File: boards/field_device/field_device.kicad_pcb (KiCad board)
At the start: 4 copper layers, 58 parts, among them J1 Conn_01x05_Pin, SW1 SW_SPST, U1 CHT20MEMS, U2 STM32C051F6P6, U3 SPA06-003, U4 CN3163, U5 HX8001-AJC, U6 SX1262IMLTRT, Y1 Crystal_GND24

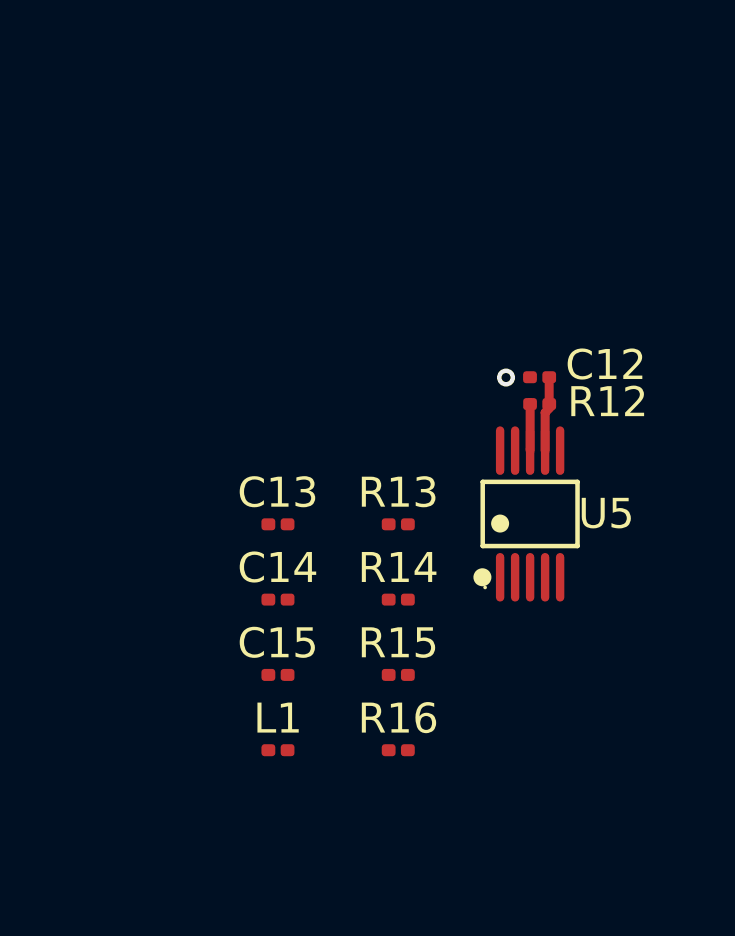
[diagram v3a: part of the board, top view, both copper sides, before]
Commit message: added sources + some pcb routing
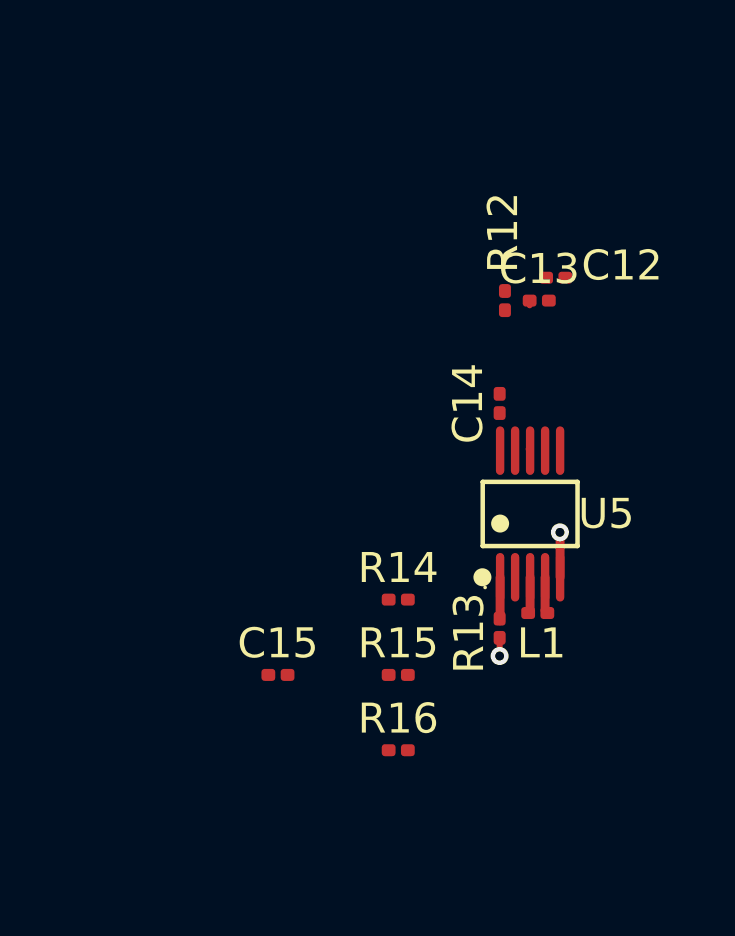
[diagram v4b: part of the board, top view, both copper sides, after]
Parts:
- moved C13 11.5 mm to (204.8, 79.2)
- moved C14 9.87 mm to (203.5, 82.7), turned to 90 degrees
- moved L1 9.79 mm to (204.7, 89.7), turned to 180 degrees
- moved R13 4.84 mm to (203.5, 90.2), turned to -90 degrees
- moved R12 3.64 mm to (203.6, 79.2), turned to -90 degrees
- moved C12 3.36 mm to (205.3, 78.5)
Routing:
- net /power_source/regulator/pwr: track 2.39 -> 0.05 mm
- net GND: track 0.00 -> 2.23 mm, vias 0 -> 2
- net /power_source/regulator/enable: track 1.71 -> 0.23 mm
- net Net-(U5-RT): track 0.00 -> 1.48 mm
- net Net-(U5-SW2): track 0.00 -> 1.22 mm
- net Net-(U5-SW1): track 0.00 -> 1.22 mm
- net (no net): vias 1 -> 0
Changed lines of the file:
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@@
 	(footprint "Capacitor_SMD:C_0201_0603Metric"
 		(layer "F.Cu")
-		(at 196.065 86.705)
+		(at 204.7748 79.248)
 		(descr "Capacitor SMD 0201 (0603 Metric), square (rectangular) end terminal, IPC-7351 nominal, (Body size source: https://www.vishay.com/docs/20052/crcw0201e3.pdf)")
 		(tags "capacitor")
@@
 		(property "Value" "100nF"
 			(at 0 1.05 0)
-			(layer "F.Fab")
+			(layer "B.Fab")
 			(effects
 				(font
@@
 					(thickness 0.15)
 				)
+				(justify mirror)
 			)
 		)
@@
 	(footprint "Resistor_SMD:R_0201_0603Metric"
 		(layer "F.Cu")
-		(at 204.787849 82.697014 180)
+		(at 203.6318 79.248 -90)
 		(descr "Resistor SMD 0201 (0603 Metric), square (rectangular) end terminal, IPC-7351 nominal, (Body size source: https://www.vishay.com/docs/20052/crcw0201e3.pdf)")
 		(tags "resistor")
 		(property "Reference" "R12"
-			(at -2.26994 0.060373 0)
+			(at -2.26994 0.060373 90)
 			(layer "F.SilkS")
 			(effects
@@
 		)
 		(property "Value" "1MΩ"
-			(at 0 1.05 0)
+			(at 0 1.05 90)
 			(layer "F.Fab")
 			(effects
@@
 		)
 		(property "Datasheet" ""
-			(at 0 0 0)
+			(at 0 0 90)
 			(layer "F.Fab")
 			(hide yes)
@@
 		)
 		(property "Description" "Resistor"
-			(at 0 0 0)
+			(at 0 0 90)
 			(layer "F.Fab")
 			(hide yes)
@@
 		)
 		(property "KiLib_Generator" "SMD_2terminal_chip_molded"
-			(at 0 0 0)
+			(at 0 0 90)
 			(layer "F.SilkS")
 			(hide yes)
@@
 		)
 		(fp_text user "${REFERENCE}"
-			(at 0 -0.68 0)
+			(at 0 -0.68 90)
 			(layer "F.Fab")
 			(effects
@@
 		)
 		(pad "" smd roundrect
-			(at -0.345 0 180)
+			(at -0.345 0 270)
 			(size 0.318 0.36)
 			(layers "F.Paste")
@@
 		)
 		(pad "" smd roundrect
-			(at 0.345 0 180)
+			(at 0.345 0 270)
 			(size 0.318 0.36)
 			(layers "F.Paste")
@@
 		)
 		(pad "1" smd roundrect
-			(at -0.32 0 180)
+			(at -0.32 0 270)
 			(size 0.46 0.4)
 			(layers "F.Cu" "F.Mask")
@@
 		)
 		(pad "2" smd roundrect
-			(at 0.32 0 180)
+			(at 0.32 0 270)
 			(size 0.46 0.4)
 			(layers "F.Cu" "F.Mask")
@@
 	(footprint "Capacitor_SMD:C_0201_0603Metric"
 		(layer "F.Cu")
-		(at 196.065 89.215)
+		(at 203.454 82.677 90)
 		(descr "Capacitor SMD 0201 (0603 Metric), square (rectangular) end terminal, IPC-7351 nominal, (Body size source: https://www.vishay.com/docs/20052/crcw0201e3.pdf)")
 		(tags "capacitor")
 		(property "Reference" "C14"
-			(at 0 -1.05 0)
+			(at 0 -1.05 90)
 			(layer "F.SilkS")
 			(effects
@@
 		)
 		(property "Value" "1.5nF"
-			(at 0 1.05 0)
+			(at 0 1.05 90)
 			(layer "F.Fab")
 			(effects
@@
 		)
 		(property "Datasheet" ""
-			(at 0 0 0)
+			(at 0 0 90)
 			(layer "F.Fab")
 			(hide yes)
@@
 		)
 		(property "Description" "Unpolarized capacitor"
-			(at 0 0 0)
+			(at 0 0 90)
 			(layer "F.Fab")
 			(hide yes)
@@
 		)
 		(property "KiLib_Generator" "SMD_2terminal_chip_molded"
-			(at 0 0 0)
+			(at 0 0 90)
 			(layer "F.SilkS")
 			(hide yes)
@@
 		)
 		(fp_text user "${REFERENCE}"
-			(at 0 -0.68 0)
+			(at 0 -0.68 90)
 			(layer "F.Fab")
 			(effects
@@
 		)
 		(pad "" smd roundrect
-			(at -0.345 0)
+			(at -0.345 0 90)
 			(size 0.318 0.36)
 			(layers "F.Paste")
@@
 		)
 		(pad "" smd roundrect
-			(at 0.345 0)
+			(at 0.345 0 90)
 			(size 0.318 0.36)
 			(layers "F.Paste")
@@
 		)
 		(pad "1" smd roundrect
-			(at -0.32 0)
+			(at -0.32 0 90)
 			(size 0.46 0.4)
 			(layers "F.Cu" "F.Mask")
@@
 		)
 		(pad "2" smd roundrect
-			(at 0.32 0)
+			(at 0.32 0 90)
 			(size 0.46 0.4)
 			(layers "F.Cu" "F.Mask")
@@
 	(footprint "Capacitor_SMD:C_0201_0603Metric"
 		(layer "F.Cu")
-		(at 204.785554 81.803054 180)
+		(at 205.323 78.486 180)
 		(descr "Capacitor SMD 0201 (0603 Metric), square (rectangular) end terminal, IPC-7351 nominal, (Body size source: https://www.vishay.com/docs/20052/crcw0201e3.pdf)")
 		(tags "capacitor")
@@
 	(footprint "Inductor_SMD:L_0201_0603Metric"
 		(layer "F.Cu")
-		(at 196.065 94.235)
+		(at 204.724 89.662 180)
 		(descr "Inductor SMD 0201 (0603 Metric), square (rectangular) end terminal, IPC-7351 nominal, (Body size source: https://www.vishay.com/docs/20052/crcw0201e3.pdf)")
 		(tags "inductor")
 		(property "Reference" "L1"
-			(at 0 -1.05 0)
+			(at -0.127 -1.016 0)
 			(layer "F.SilkS")
 			(effects
@@
 		)
 		(pad "" smd roundrect
-			(at -0.345 0)
+			(at -0.345 0 180)
 			(size 0.318 0.36)
 			(layers "F.Paste")
@@
 		)
 		(pad "" smd roundrect
-			(at 0.345 0)
+			(at 0.345 0 180)
 			(size 0.318 0.36)
 			(layers "F.Paste")
@@
 		)
 		(pad "1" smd roundrect
-			(at -0.32 0)
+			(at -0.32 0 180)
 			(size 0.46 0.4)
 			(layers "F.Cu" "F.Mask")
@@
 		)
 		(pad "2" smd roundrect
-			(at 0.32 0)
+			(at 0.32 0 180)
 			(size 0.46 0.4)
 			(layers "F.Cu" "F.Mask")
@@
 	(footprint "Resistor_SMD:R_0201_0603Metric"
 		(layer "F.Cu")
-		(at 200.075 86.705)
+		(at 203.454 90.17 -90)
 		(descr "Resistor SMD 0201 (0603 Metric), square (rectangular) end terminal, IPC-7351 nominal, (Body size source: https://www.vishay.com/docs/20052/crcw0201e3.pdf)")
 		(tags "resistor")
 		(property "Reference" "R13"
-			(at 0 -1.05 0)
+			(at 0.163 1.016 90)
 			(layer "F.SilkS")
 			(effects
@@
 		)
 		(property "Value" "60.4kΩ"
-			(at 0 1.05 0)
+			(at 0 1.05 90)
 			(layer "F.Fab")
 			(effects
@@
 		)
 		(property "Datasheet" ""
-			(at 0 0 0)
+			(at 0 0 90)
 			(layer "F.Fab")
 			(hide yes)
@@
 		)
 		(property "Description" "Resistor"
-			(at 0 0 0)
+			(at 0 0 90)
 			(layer "F.Fab")
 			(hide yes)
@@
 		)
 		(property "KiLib_Generator" "SMD_2terminal_chip_molded"
-			(at 0 0 0)
+			(at 0 0 90)
 			(layer "F.SilkS")
 			(hide yes)
@@
 		)
 		(fp_text user "${REFERENCE}"
-			(at 0 -0.68 0)
+			(at 0 -0.68 90)
 			(layer "F.Fab")
 			(effects
@@
 		)
 		(pad "" smd roundrect
-			(at -0.345 0)
+			(at -0.345 0 270)
 			(size 0.318 0.36)
 			(layers "F.Paste")
@@
 		)
 		(pad "" smd roundrect
-			(at 0.345 0)
+			(at 0.345 0 270)
 			(size 0.318 0.36)
 			(layers "F.Paste")
@@
 		)
 		(pad "1" smd roundrect
-			(at -0.32 0)
+			(at -0.32 0 270)
 			(size 0.46 0.4)
 			(layers "F.Cu" "F.Mask")
@@
 		)
 		(pad "2" smd roundrect
-			(at 0.32 0)
+			(at 0.32 0 270)
 			(size 0.46 0.4)
 			(layers "F.Cu" "F.Mask")
@@
 		)
 	)
-	(via blind
-		(at 203.667585 81.812532)
-		(size 0.6)
-		(drill 0.3)
-		(layers "F.Cu" "In1.Cu")
-		(net "")
+	(segment
+		(start 204.9572 84.2372)
+		(end 204.97 84.25)
+		(width 0.2)
+		(layer "F.Cu")
+		(net "/power_source/regulator/pwr")
 	)
 	(segment
-		(start 205.105554 81.803054)
-		(end 205.105554 82.694719)
-		(width 0.3)
+		(start 204.9932 84.2268)
+		(end 204.97 84.25)
+		(width 0.2)
 		(layer "F.Cu")
 		(net "/power_source/regulator/pwr")
 	)
 	(segment
-		(start 205.132849 82.818361)
-		(end 204.97 82.98121)
+		(start 205.47 87.138)
+		(end 205.47 88.47)
 		(width 0.3)
 		(layer "F.Cu")
-		(net "/power_source/regulator/pwr")
+		(net "GND")
+	)
+	(segment
+		(start 205.463539 86.973212)
+		(end 205.463539 87.131539)
+		(width 0.3)
+		(layer "F.Cu")
+		(net "GND")
 	)
 	(segment
-		(start 205.105554 82.694719)
-		(end 205.107849 82.697014)
+		(start 203.454 90.581)
+		(end 203.454 91.186)
 		(width 0.2)
 		(layer "F.Cu")
-		(net "/power_source/regulator/pwr")
+		(net "GND")
 	)
 	(segment
-		(start 204.97 82.98121)
-		(end 204.97 84.25)
+		(start 205.463539 87.131539)
+		(end 205.47 87.138)
 		(width 0.3)
 		(layer "F.Cu")
-		(net "/power_source/regulator/pwr")
+		(net "GND")
+	)
+	(segment
+		(start 205.0948 78.5778)
+		(end 205.003 78.486)
+		(width 0.2)
+		(layer "F.Cu")
+		(net "GND")
+	)
+	(via blind
+		(at 203.454 91.095)
+		(size 0.6)
+		(drill 0.3)
+		(layers "F.Cu" "In1.Cu")
+		(net "GND")
+	)
+	(via blind
+		(at 205.463539 86.973212)
+		(size 0.6)
+		(drill 0.3)
+		(layers "F.Cu" "In1.Cu")
+		(net "GND")
 	)
 	(segment
@@
 	)
 	(segment
-		(start 204.47 82.641211)
-		(end 204.492849 82.618362)
+		(start 204.4548 79.248)
+		(end 204.4548 79.406456)
 		(width 0.2)
 		(layer "F.Cu")
@@
 	)
 	(segment
-		(start 204.47 84.25)
-		(end 204.47 82.641211)
+		(start 204.97 88.47)
+		(end 204.97 89.588)
 		(width 0.3)
 		(layer "F.Cu")
-		(net "/power_source/regulator/enable")
+		(net "Net-(U5-SW2)")
+	)
+	(segment
+		(start 204.97 89.588)
+		(end 205.044 89.662)
+		(width 0.2)
+		(layer "F.Cu")
+		(net "Net-(U5-SW2)")
+	)
+	(segment
+		(start 204.47 89.596)
+		(end 204.404 89.662)
+		(width 0.2)
+		(layer "F.Cu")
+		(net "Net-(U5-SW1)")
+	)
+	(segment
+		(start 204.47 88.47)
+		(end 204.47 89.596)
+		(width 0.3)
+		(layer "F.Cu")
+		(net "Net-(U5-SW1)")
+	)
+	(segment
+		(start 203.47 88.47)
+		(end 203.47 89.925)
+		(width 0.3)
+		(layer "F.Cu")
+		(net "Net-(U5-RT)")
+	)
+	(segment
+		(start 203.47 89.925)
+		(end 203.454 89.941)
+		(width 0.2)
+		(layer "F.Cu")
+		(net "Net-(U5-RT)")
 	)
 	(zone

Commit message: i guess made schematic more readable?
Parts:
- removed C24: C_Shunt_1, Capacitor_SMD:C_0603_1608Metric
- removed C25: C_Shunt_2, Capacitor_SMD:C_0603_1608Metric
- removed D1: LED, LED_SMD:LED_0603_1608Metric
- removed L1: 10uH, Inductor_SMD:L_0201_0603Metric
- removed R10: 1kΩ, Resistor_SMD:R_0603_1608Metric
- removed R15: 15kΩ, Resistor_SMD:R_0201_0603Metric
- removed R16: 200kΩ, Resistor_SMD:R_0201_0603Metric
- removed R5: 10kΩ, Resistor_SMD:R_0603_1608Metric
- removed R9: 10kΩ?, Resistor_SMD:R_0603_1608Metric
- added D3: GREEN, LED_SMD:LED_0603_1608Metric, F.Cu at (32.8, 48.1)
- added J2: Conn_01x02_Pin, Connector_PinHeader_1.00mm:PinHeader_1x02_P1.00mm_Vertical, F.Cu at (39.7, 13.3)
- C1: value 10uF -> 10u
- C10: value 1uF -> 10u; footprint Capacitor_SMD:C_0603_1608Metric -> Capacitor_SMD:C_0201_0603Metric
- C11: value 1uF -> 100n; footprint Capacitor_SMD:C_0603_1608Metric -> Sensor_Current:LEM_HX02-P
- C12: value 10uF -> 22u; footprint Capacitor_SMD:C_0201_0603Metric -> Sensor_Current:LEM_HX02-P
- C13: value 100nF -> 1n5; footprint Capacitor_SMD:C_0201_0603Metric -> Sensor_Current:LEM_HX02-P
- C14: value 1.5nF -> 10uF; footprint Capacitor_SMD:C_0201_0603Metric -> Capacitor_SMD:C_0603_1608Metric
- C15: value 22uF -> 100nF; footprint Capacitor_SMD:C_0201_0603Metric -> Capacitor_SMD:C_0603_1608Metric
- C16: value 470nF -> 100nF
- C17: value 10uF -> 100nF
- C18: value 100nF -> 470nF
- C19: value 100nF -> 47nF
- C2: value 4.7uF -> 100n
- C20: value 100nF -> 100pF
- C21: value 47nF -> 100pF
- C22: value 100pF -> C_Shunt_1
- C23: value 100pF -> C_Shunt_2
- C3: value 100nF -> 10u
- C4, C5, C6, C7: value 100nF -> 100n
- C8, C9: value 100nF -> 1u
- D2: value LED -> ORANGE
- R1: value 330Ω -> 330R
- R11: value 2kΩ -> 10k
- R12: value 1MΩ -> 10k?; footprint Resistor_SMD:R_0201_0603Metric -> Resistor_SMD:R_0603_1608Metric
- R13: value 60.4kΩ -> 1kΩ; footprint Resistor_SMD:R_0201_0603Metric -> Resistor_SMD:R_0603_1608Metric
- R14: value 340kΩ -> 1k5; footprint Resistor_SMD:R_0201_0603Metric -> Resistor_SMD:R_0603_1608Metric
- R2: value 10kΩ? -> 10k
- R3: value 10kΩ -> 10k
- R4: value 10kΩ -> 10k?
- R6, R7, R8: value 22Ω -> 22R
- U2: value STM32C051F6P6 -> STM32C011F6Px; footprint LCSC downloads:TSSOP-20_L6.5-W4.4-P0.65-LS6.4-BL -> Package_SO:TSSOP-20_4.4x6.5mm_P0.65mm
- moved C12 209.8 mm to (3.42, 21.4), turned to 0 degrees
- moved C13 205.4 mm to (3.42, 38.5)
- moved U5 200.1 mm to (22.6, 2.92)
- moved C14 185.9 mm to (28.7, 19.1), turned to 0 degrees
- moved C15 181.4 mm to (28.7, 21.6)
- moved R13 181.1 mm to (28.7, 42.5), turned to 0 degrees
- moved R14 177.0 mm to (28.7, 45.0)
- moved C11 173.5 mm to (3.42, 4.31)
- moved C8 163.5 mm to (28.7, 37.5)
- moved C9 163.5 mm to (28.7, 40.0)
- moved R12 163.2 mm to (43.1, 49.8), turned to 0 degrees
- moved C10 155.5 mm to (21.4, 7.21)
- moved AE1 154.4 mm to (40.8, 30.2)
- moved L2 154.4 mm to (36.8, 24.1)
- moved L3 154.4 mm to (36.8, 26.6)
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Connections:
- net /MCU/prgm_clk renamed /MCU/SWDCLK
- net /MCU/prgm_io renamed /MCU/SWDIO
- BT1 pad 1: /power_source/regulator/pwr -> VBUS
- C10 pad 1: /power_source/solar_pwr -> VBUS
- C11 pad 1: /power_source/regulator/pwr -> /power_source/regulator/EN
- C12 pad 1: /power_source/regulator/pwr -> +3.3V
- C13 pad 1: /power_source/regulator/enable -> Net-(C13-Pad1)
- C13 pad 2: GND -> Net-(U5-VC)
- C14 pad 1: Net-(U5-VC) -> +3.3V
- C14 pad 2: Net-(C14-Pad2) -> GND
- C16 pad 1: Net-(U6-VREG) -> +3.3V
- C18 pad 1: +3.3V -> Net-(U6-VREG)
- C19 pad 1: +3.3V -> Net-(U6-VR_PA)
- C2 pad 1: +3.3V -> /MCU/NRST
- C20 pad 1: /lora_module/VDD_RADIO -> Net-(U6-VR_PA)
- C21 pad 1: Net-(U6-VR_PA) -> Net-(C21-Pad1)
- C21 pad 2: GND -> Net-(U6-RFO)
- C22 pad 1: Net-(U6-VR_PA) -> Net-(C21-Pad1)
- C23 pad 1: Net-(C23-Pad1) -> Net-(AE1-A)
- C23 pad 2: Net-(U6-RFO) -> GND
- C5 pad 1: /MCU/prgm_nrst -> +3.3V
- C8 pad 1: +3.3V -> /power_source/solar_pwr
- C9 pad 1: +3.3V -> VBUS
- D2 pad 1: /power_source/done -> /power_source/chrg
- D2 pad 2: Net-(D1-A) -> Net-(D2-A)
- J1 pad 5: /MCU/prgm_nrst -> /MCU/NRST
- L3 pad 1: Net-(C23-Pad1) -> Net-(C21-Pad1)
- R11 pad 1: Net-(U4-ISET) -> /MCU/RF_NSS
- R11 pad 2: GND -> +3.3V
- R12 pad 1: /power_source/regulator/pwr -> +3.3V
- R12 pad 2: /power_source/regulator/enable -> Net-(U3-CSB)
- R13 pad 1: Net-(U5-RT) -> /power_source/solar_pwr
- R13 pad 2: GND -> Net-(D2-A)
- R14 pad 1: Net-(U5-FB) -> Net-(U4-ISET)
- R14 pad 2: +3.3V -> GND
- R2 pad 1: +3.3V -> /MCU/SDA_bus
- R2 pad 2: /MCU/prgm_nrst -> +3.3V
- R3 pad 1: /MCU/SDA_bus -> /MCU/SCL_bus
- R4 pad 1: /MCU/SCL_bus -> +3.3V
- R4 pad 2: +3.3V -> /MCU/NRST
- R6 pad 1: Net-(U2-PA7) -> /MCU/RF_SCK
- R6 pad 2: /MCU/RF_MOSI -> /MCU/RF_SCK
- R7 pad 1: Net-(U2-PA6) -> /MCU/RF_MISO
- R8 pad 1: Net-(U2-PA5) -> /MCU/RF_MOSI
- R8 pad 2: /MCU/RF_SCK -> /MCU/RF_MOSI
- SW1 pad 2: /MCU/prgm_nrst -> /MCU/NRST
- U2 pad 12: Net-(U2-PA5) -> /MCU/RF_SCK
- U2 pad 13: Net-(U2-PA6) -> /MCU/RF_MISO
- U2 pad 14: Net-(U2-PA7) -> /MCU/RF_MOSI
- U2 pad 15: unconnected-(U2-PA8-Pad15) -> Net-(U2-PA8)
- U2 pad 16: unconnected-(U2-PA11[PA9]-Pad16) -> /MCU/LOG_MCU_TX
- U2 pad 17: unconnected-(U2-PA12[PA10]-Pad17) -> /MCU/LOG_MCU_RX
- U2 pad 6: /MCU/prgm_nrst -> /MCU/NRST
- U4 pad 5: /power_source/regulator/pwr -> VBUS
- U4 pad 8: /power_source/regulator/pwr -> VBUS
- U5 pad 1: Net-(U5-RT) -> /power_source/regulator/RT
- U5 pad 2: GND -> unconnected-(U5-MS-Pad2)
- U5 pad 4: Net-(U5-SW2) -> /power_source/regulator/L
- U5 pad 7: /power_source/regulator/pwr -> VBUS
- U5 pad 8: /power_source/regulator/enable -> /power_source/regulator/EN
- U5 pad 9: Net-(U5-FB) -> /power_source/regulator/FB_NETWORK
- U6 pad 1: /lora_module/VDD_RADIO -> +3.3V
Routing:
- net GND: track 2.23 -> 0.00 mm, vias 2 -> 0
- net Net-(U5-RT): track 1.48 -> 0.00 mm
- net Net-(U5-SW2): track 1.22 -> 0.00 mm
- net Net-(U5-SW1): track 1.22 -> 0.00 mm
